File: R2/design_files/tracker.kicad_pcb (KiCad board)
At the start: 4 copper layers, 49.4 x 53.4 mm, 95 parts, among them J1 Conn_01x01, J2 Conn_01x01, J3 Conn_01x05, J4 Conn_Coaxial, J5 SIM_Card, J6 Conn_01x02, M1 BG96, Q1 DMP2008UFG, U1 STM32U545CEUx, U10 PUMH10,115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

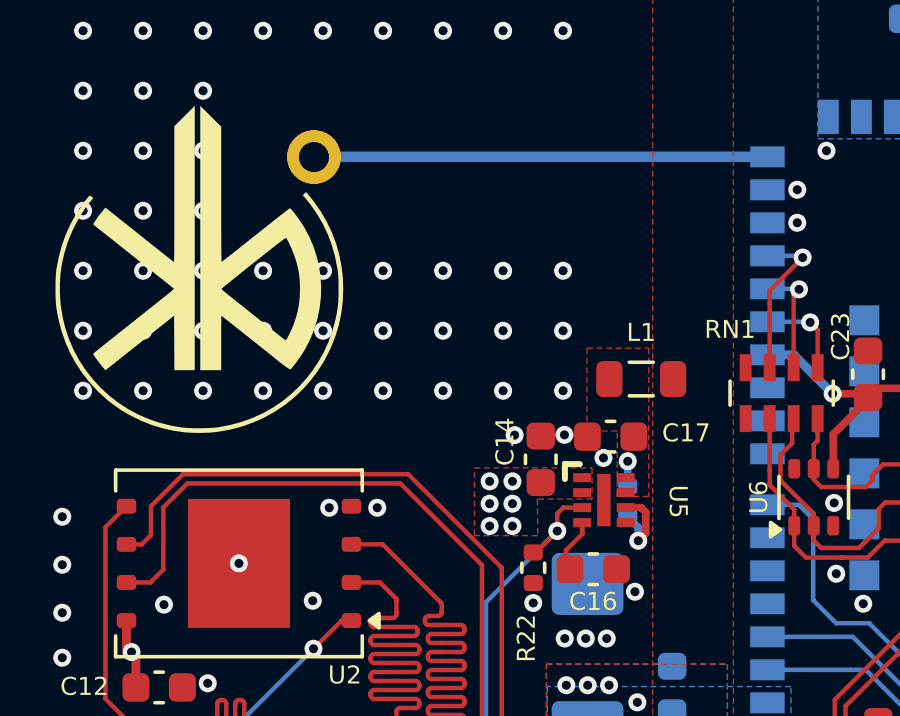
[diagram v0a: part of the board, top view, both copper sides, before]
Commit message: added capacitor 470u
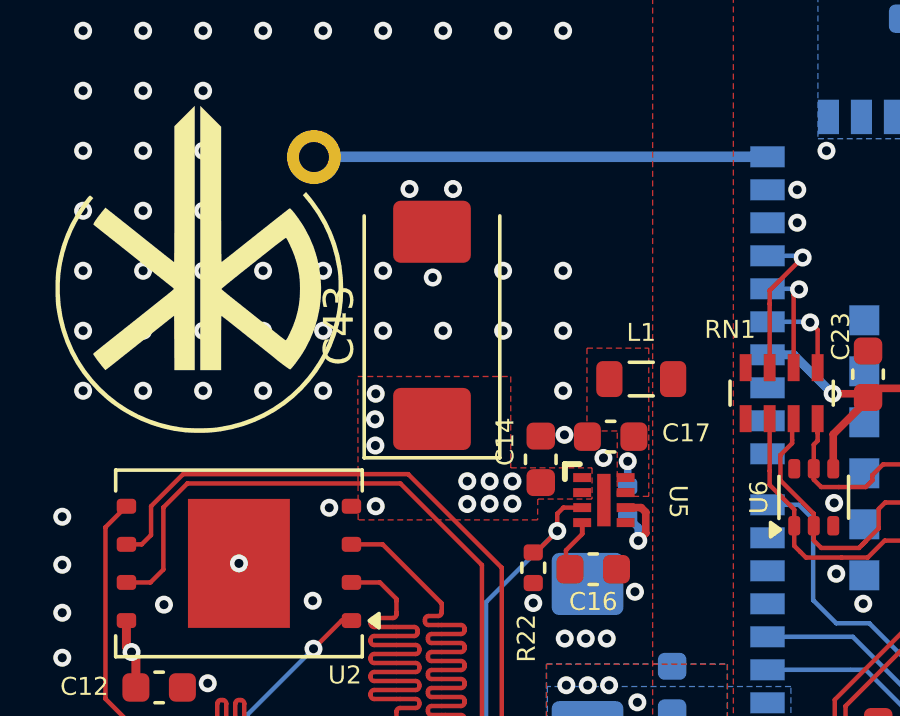
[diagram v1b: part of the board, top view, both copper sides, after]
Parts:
- added C43: 470u, Capacitor_Tantalum_SMD:CP_EIA-7343-31_Kemet-D, F.Cu at (138.4, 58.5)
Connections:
- U13 pad 1: unconnected-(U13-Pad1) -> GND
- U4 pad 20: /gsm/GSM_STATUS -> unconnected-(U4-B1-Pad20)
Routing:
- net GND: vias 319 -> 317
- net +VSYS: vias 18 -> 21
